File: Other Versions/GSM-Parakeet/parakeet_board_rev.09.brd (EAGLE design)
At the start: 33.5 x 38.5 mm, 15 parts

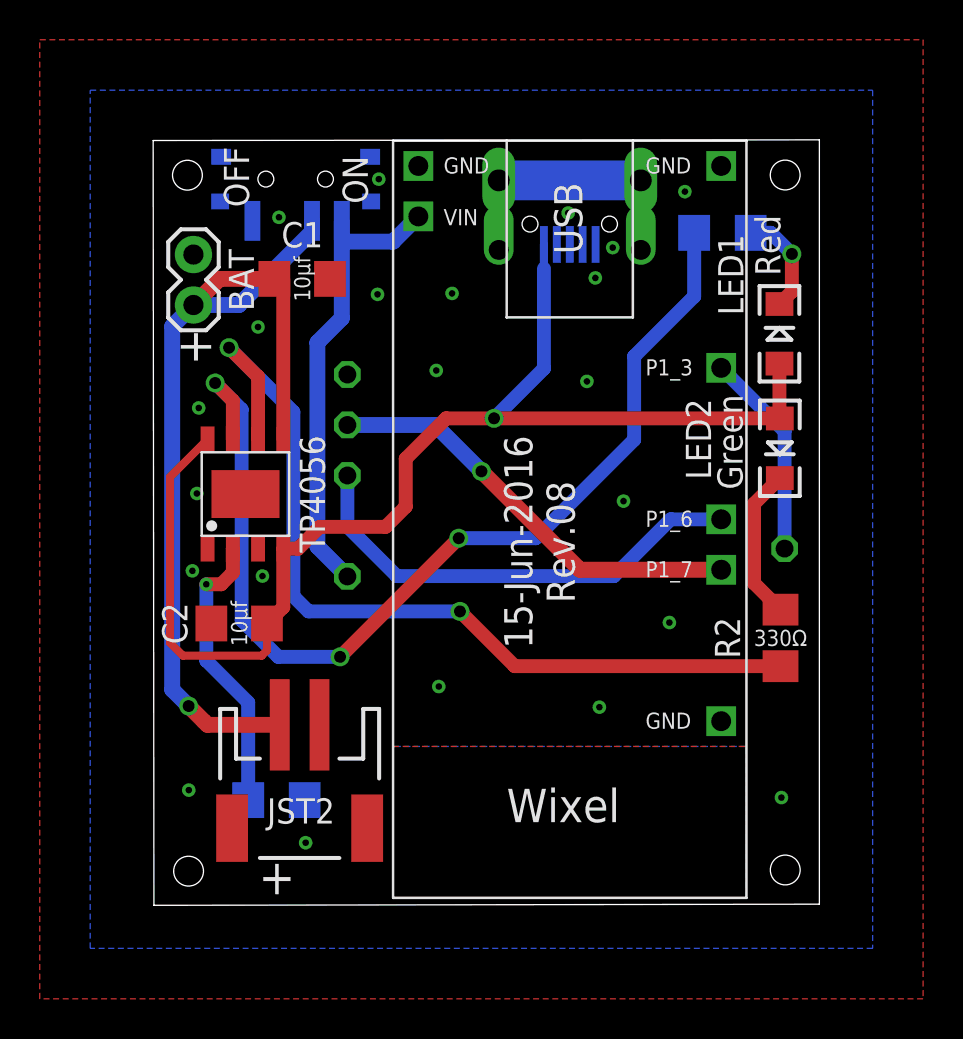
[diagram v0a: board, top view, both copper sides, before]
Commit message: Updated Parakeet rev.09
Fixed SIM800 module dimensions
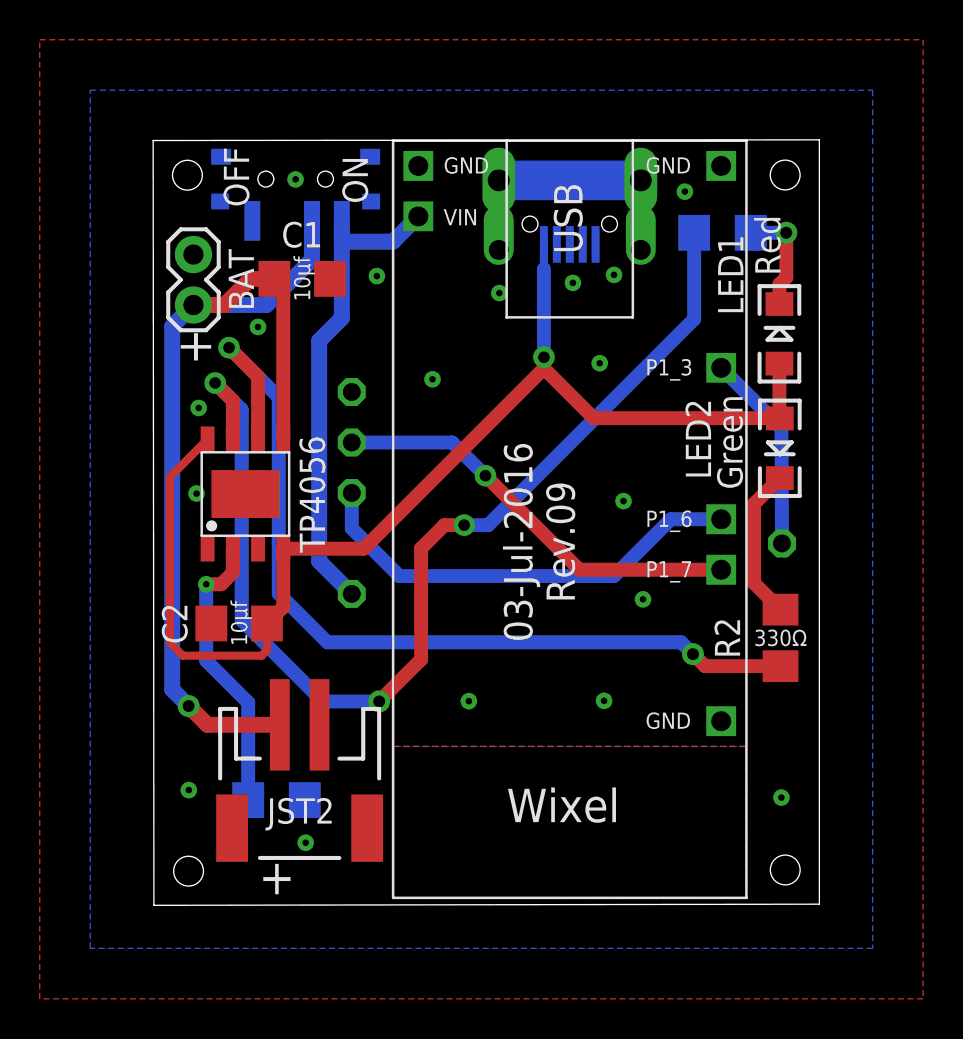
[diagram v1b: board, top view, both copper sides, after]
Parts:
- moved SIM800L 16.1 mm to (10.1, 72.9)
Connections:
- net GND: now also SIM800L.P$6_GND1; no longer SIM800L.P$6_GND
- net N$12: now also SIM800L.P$2_VIN1; no longer SIM800L.P$2_VIN
- net N$13: now also SIM800L.P$8_DTR1; no longer SIM800L.P$8_DTR
- net N$2: now also SIM800L.P$5_TXD1; no longer SIM800L.P$5_TXD
- net N$9: now also SIM800L.P$4_RXD1; no longer SIM800L.P$4_RXD
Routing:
- net N$5: track 52.4 -> 55.7 mm
- net N$7: track 63.6 -> 60.6 mm
- net N$9: track 23.6 -> 22.6 mm
- net N$12: track 23.4 -> 24.3 mm
- net N$8: track 47.1 -> 47.9 mm
- net N$2: track 21.8 -> 21.2 mm
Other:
- board text added: "03-Jul-2016 Rev.09"
- board text removed: "15-Jun-2016 Rev.08"
